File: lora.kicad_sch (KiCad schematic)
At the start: 30 parts, among them J8 S02-25200300, J9 SMA, U4 LR2021IMLTRT, Y2 TG2520SMN 32.0000M-MCGNNM0

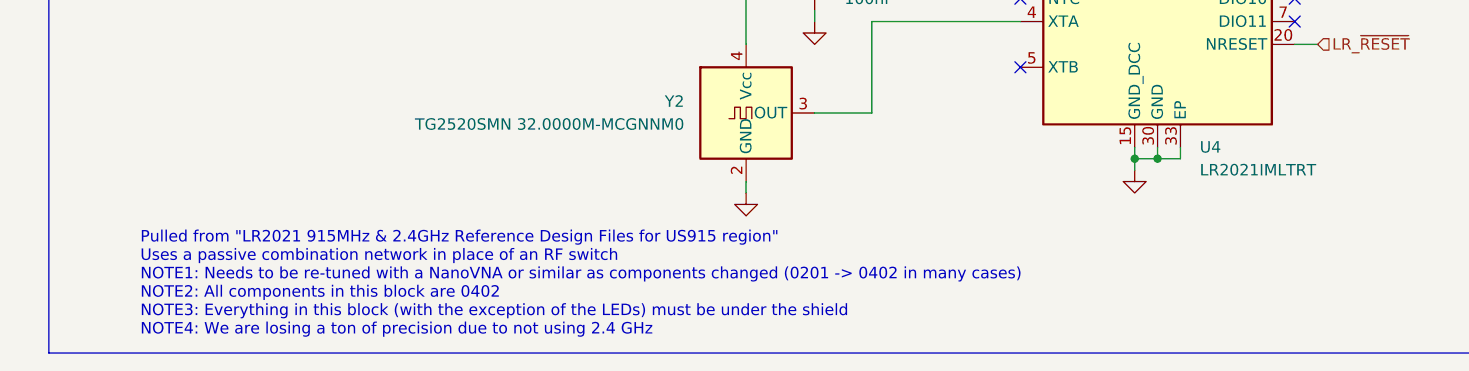
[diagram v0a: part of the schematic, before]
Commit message: Add buzzer, fix some erc
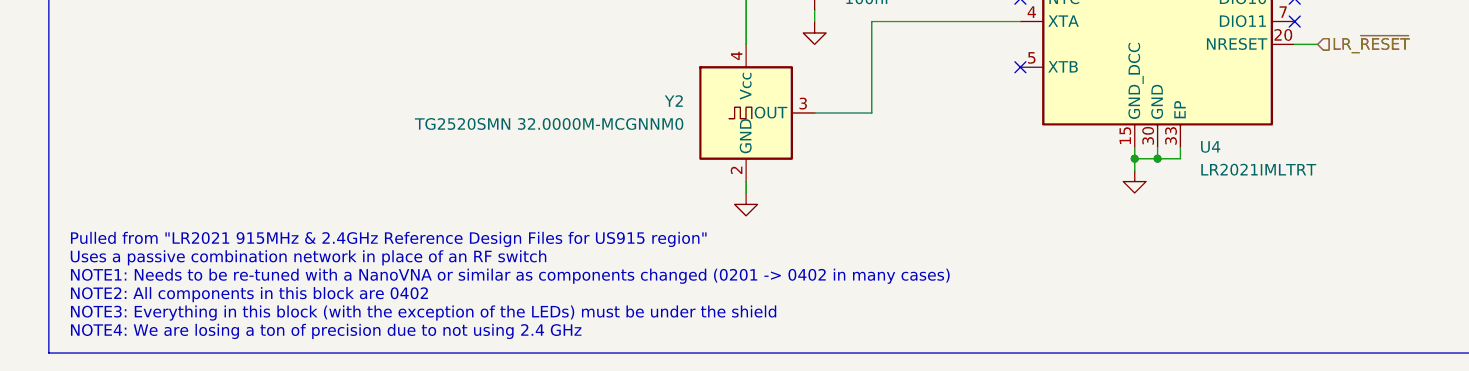
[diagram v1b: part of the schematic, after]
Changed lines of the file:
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@@
 	(text "Pulled from \"LR2021 915MHz & 2.4GHz Reference Design Files for US915 region\"\nUses a passive combination network in place of an RF switch\nNOTE1: Needs to be re-tuned with a NanoVNA or similar as components changed (0201 -> 0402 in many cases)\nNOTE2: All components in this block are 0402\nNOTE3: Everything in this block (with the exception of the LEDs) must be under the shield\nNOTE4: We are losing a ton of precision due to not using 2.4 GHz"
 		(exclude_from_sim no)
-		(at 26.67 132.08 0)
+		(at 18.796 132.334 0)
 		(effects
 			(font
